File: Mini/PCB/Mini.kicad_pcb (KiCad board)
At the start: 2 copper layers, 155.9 x 99.3 mm, 30 parts

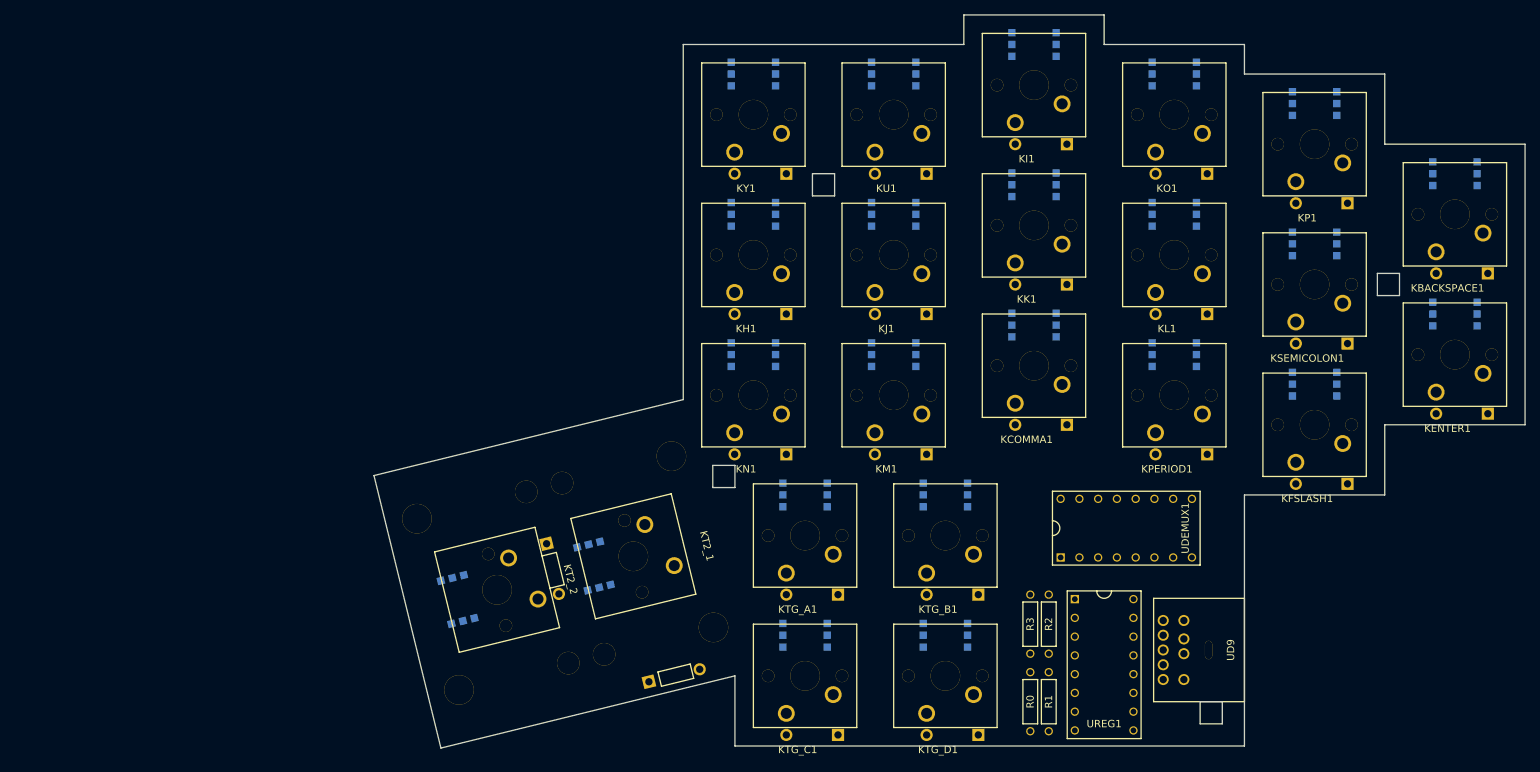
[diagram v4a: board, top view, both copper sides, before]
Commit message: Updating component footprints for proper silkscreen.  Adding LED cutouts to PCB (except for 2-key).
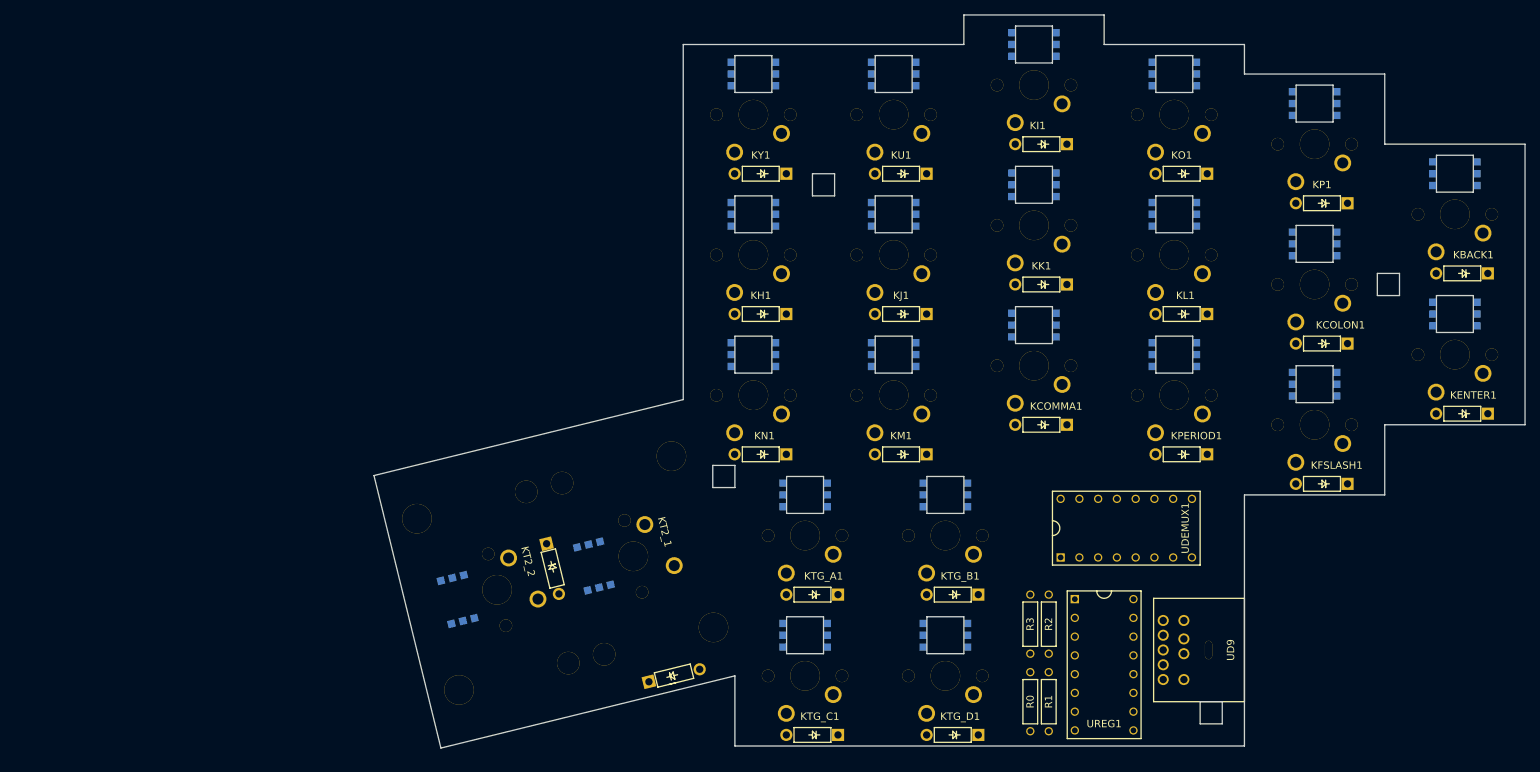
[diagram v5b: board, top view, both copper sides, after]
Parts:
- renumbered KBACKSPACE1 to KBACK1, KSEMICOLON1 to KCOLON1
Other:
- outline, holes or cut-outs redrawn
